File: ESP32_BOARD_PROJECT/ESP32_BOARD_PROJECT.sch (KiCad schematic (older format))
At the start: 0 parts

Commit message: Done power circuit and ESP32 symbol
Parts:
- added C? (x4): C, symbol Device:C
- added C?: CP, symbol Device:CP
- added J?: PJ-002A, CUI_PJ-002A, symbol PJ-002A:PJ-002A
- added L? (x2): L, symbol Device:L
- added R? (x2): R, symbol Device:R
- added U?: AMS1117-3.3, Package_TO_SOT_SMD:SOT-223-3_TabPin2, symbol Regulator_Linear:AMS1117-3.3
- added U?: AMS1117-5.0, Package_TO_SOT_SMD:SOT-223-3_TabPin2, symbol Regulator_Linear:AMS1117-5.0
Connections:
- new net: C?.1, C?.1, J?.1, U?.3 (VI), U?.3 (VI)
- new net: L?.2, R?.2 (x2)
- new net +3V3: C?.1, U?.2 (VO)
- new net +5V: C?.1, U?.2 (VO)
- new net GND: C?.2, C?.2, C?.2, C?.2, J?.2, J?.3, L?.1, L?.1, U?.1 (GND), U?.1 (GND)
- new net GNDA: R?.1
- new net GNDD: R?.1

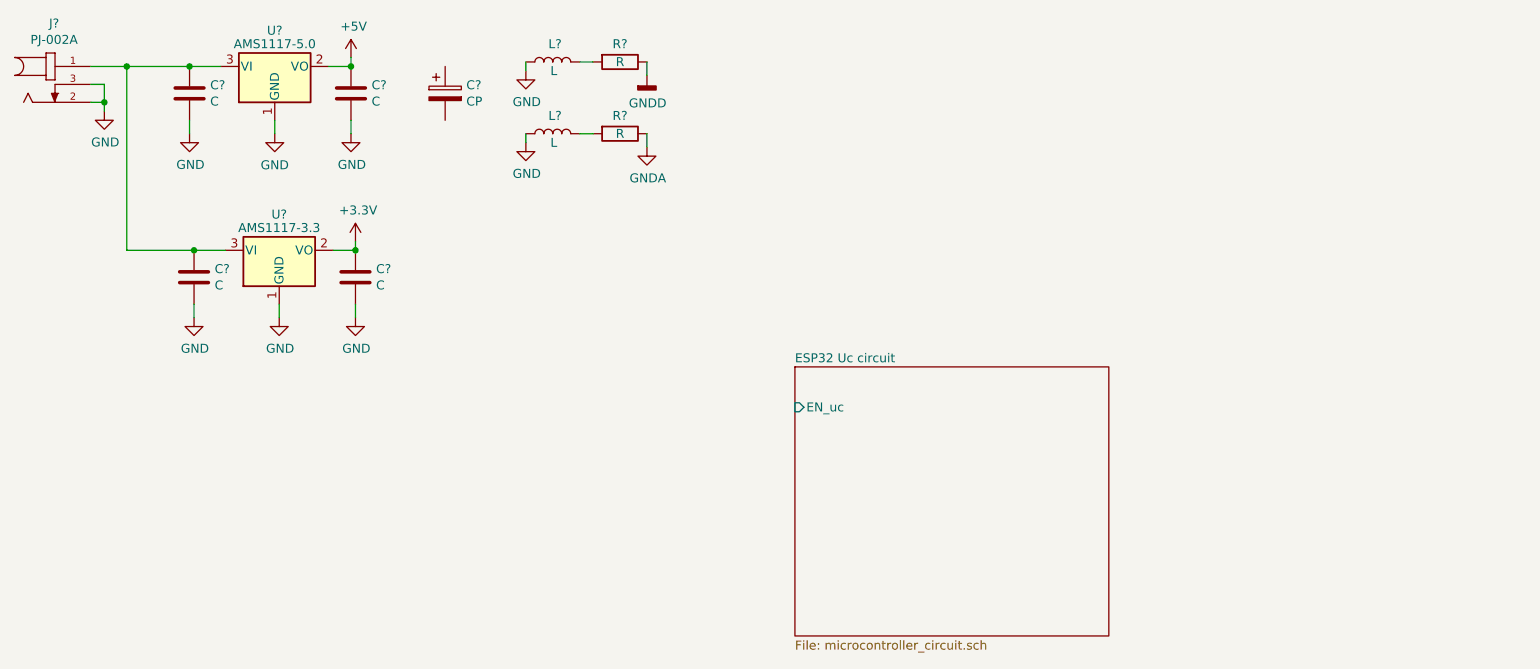
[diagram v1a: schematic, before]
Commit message: USB-Serial converter circuit half done
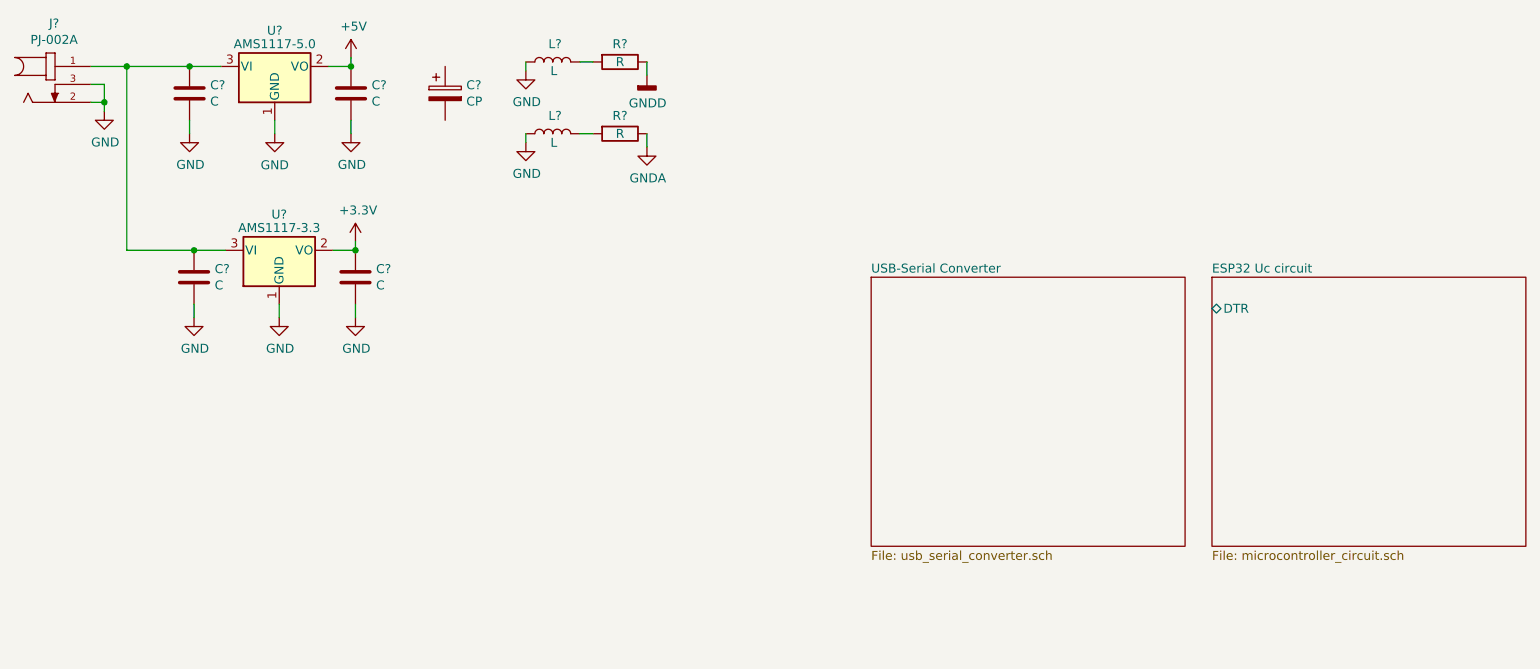
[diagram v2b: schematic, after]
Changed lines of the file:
@@
 $Descr A4 11693 8268
 encoding utf-8
-Sheet 1 2
+Sheet 1 3
 Title ""
 Date "2021-03-19"
@@
 $EndDescr
 $Sheet
-S 5000 2500 1750 1500
+S 7325 2000 1750 1500
 U 60697214
 F0 "ESP32 Uc circuit" 50
 F1 "microcontroller_circuit.sch" 50
-F2 "EN_uc" I L 5000 2725 50
+F2 "DTR" B L 7325 2175 50
 $EndSheet
 $Comp
@@
 	1    0    0    -1
 $EndComp
+$Sheet
+S 5425 2000 1750 1500
+U 606DC0A1
+F0 "USB-Serial Converter" 50
+F1 "usb_serial_converter.sch" 50
+$EndSheet
 $EndSCHEMATC
